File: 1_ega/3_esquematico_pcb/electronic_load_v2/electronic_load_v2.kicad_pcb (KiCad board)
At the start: 2 copper layers, 100 x 100 mm, 65 parts, among them J1 Encoder, J10 5V, J11 LOAD, J12 Memoria SD, J13 LCD, J14 Io_sens, J15 VCC, J17 EGB_I2C, J18 EGB_UART, J2 RTC_I2C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

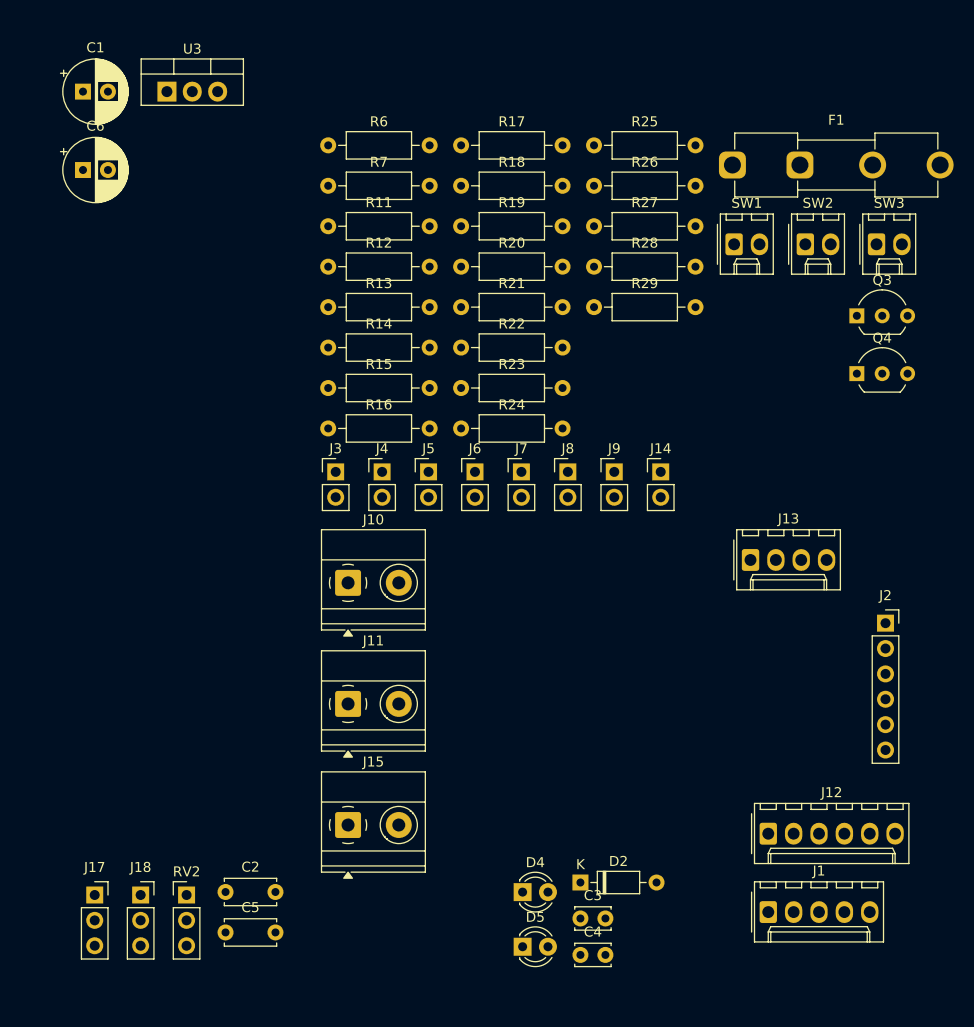
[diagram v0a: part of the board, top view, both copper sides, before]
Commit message: chore: pwm_offset con gpio
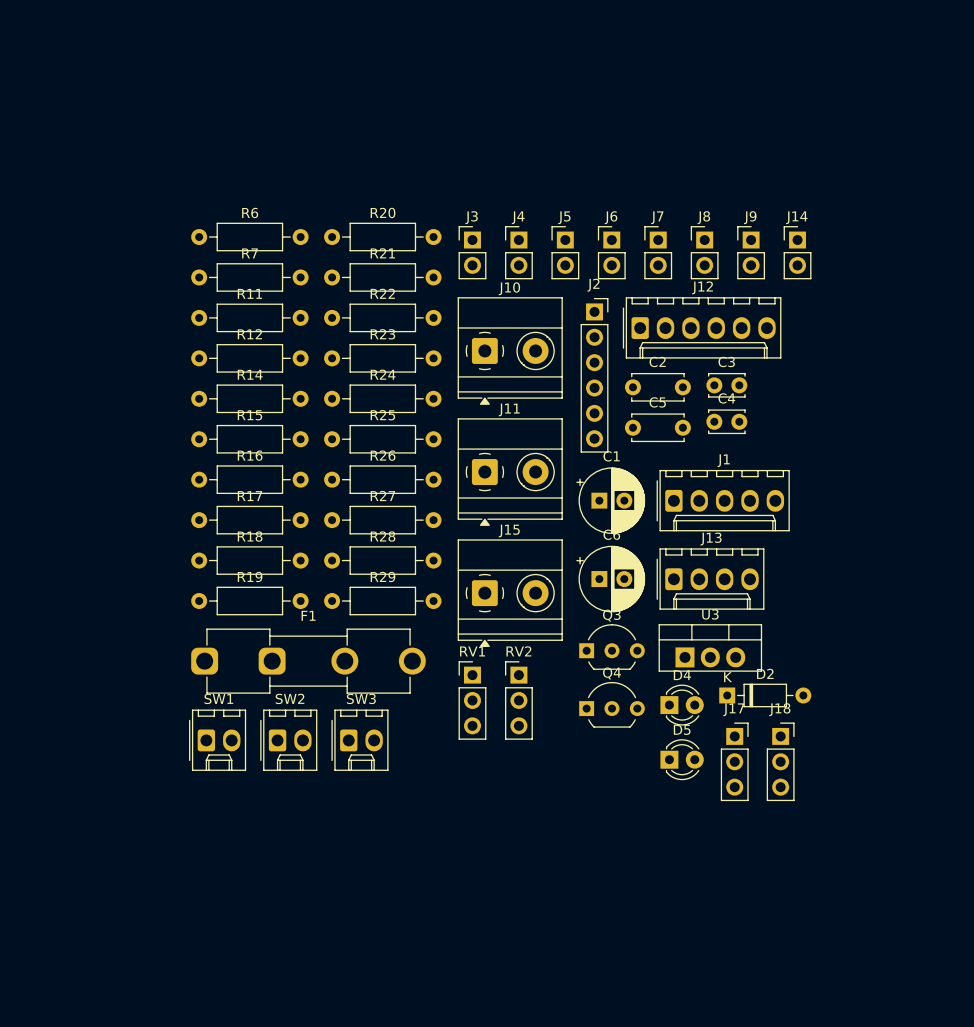
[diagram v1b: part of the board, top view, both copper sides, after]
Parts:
- removed R13: 6.8k, Resistor_THT:R_Axial_DIN0207_L6.3mm_D2.5mm_P10.16mm_Horizontal
- added RV1: 5k, Connector_PinHeader_2.54mm:PinHeader_1x03_P2.54mm_Vertical, F.Cu at (168.7, 83.9)
- R16: value 10k -> 4.7k
- moved U3 76.8 mm to (190.0, 82.1)
- moved F1 72.5 mm to (141.9, 82.5)
- moved SW1 72.5 mm to (142.1, 90.4)
- moved SW2 72.5 mm to (149.2, 90.4)
- moved SW3 72.5 mm to (156.3, 90.4)
- moved J17 66.0 mm to (195.0, 90.0)
- moved J18 66.0 mm to (199.6, 90.0)
- moved C1 66.0 mm to (181.4, 66.4)
- moved C6 66.0 mm to (181.4, 74.2)
- moved C2 65.0 mm to (184.8, 55.0)
- moved C5 65.0 mm to (184.8, 59.1)
- moved C4 55.0 mm to (192.9, 58.5)
- moved C3 55.0 mm to (192.9, 54.9)
- moved J12 52.2 mm to (185.5, 49.1)
- moved R18 45.8 mm to (141.3, 72.4)
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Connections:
- A1 pad 22: unconnected-(A1-GPIO17-Pad22) -> MOS_EN
- RV2 pad 1: Net-(R12-Pad1) -> MOS_EN
- RV2 pad 2: Net-(R12-Pad1) -> MOS_OFFSET
- RV2 pad 3: GND -> MOS_OFFSET

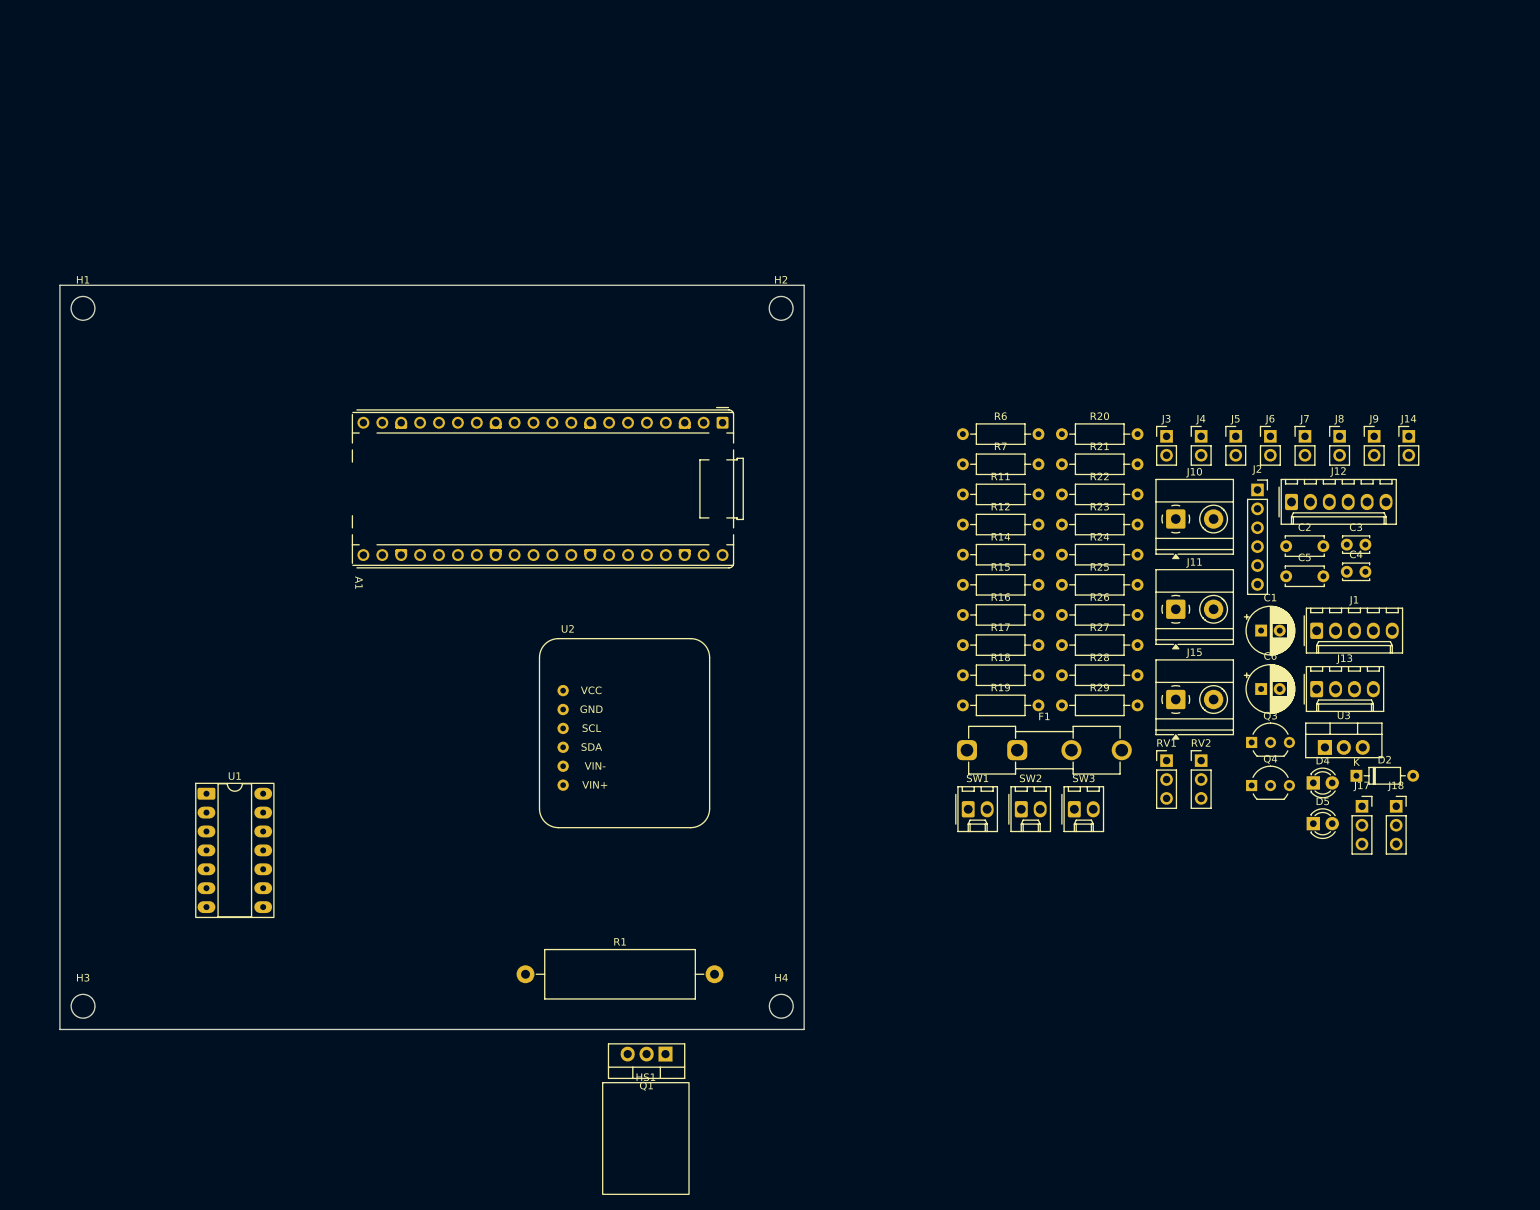
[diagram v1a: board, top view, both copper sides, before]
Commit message: perf: resistencias a huellas smd y preliminar de segunda version de pcb
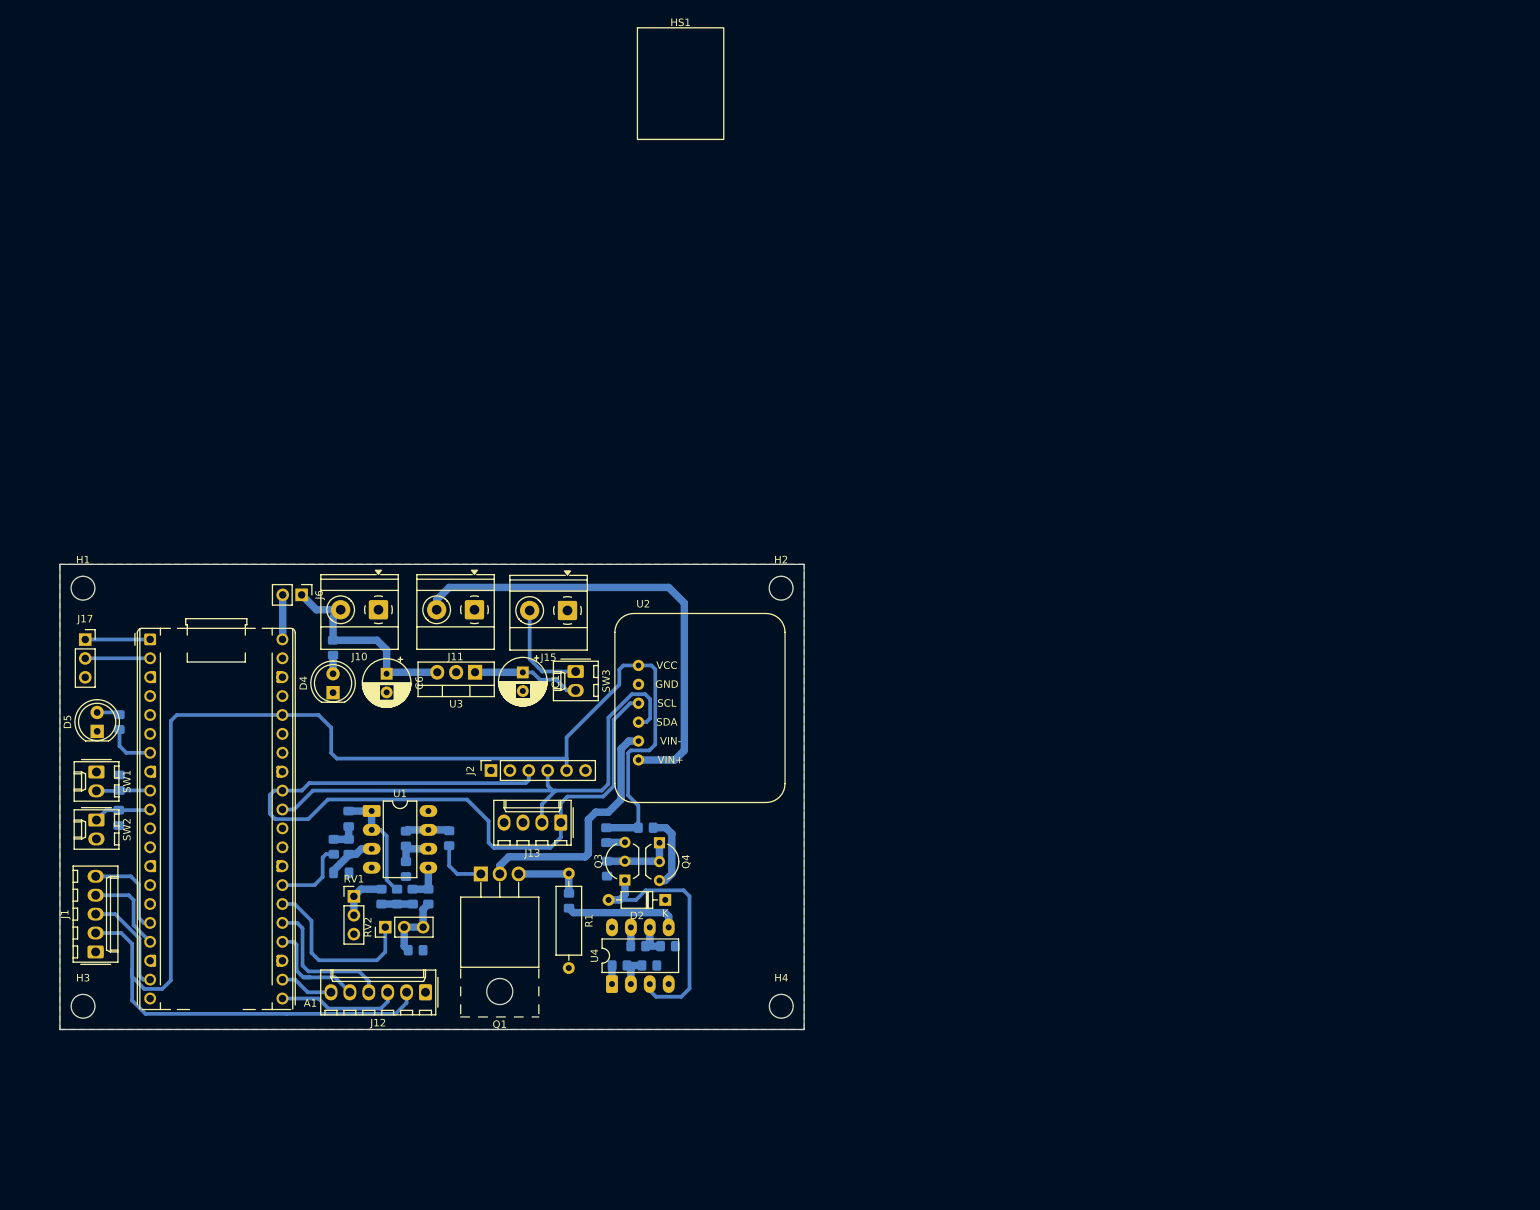
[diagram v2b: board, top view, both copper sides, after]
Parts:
- removed F1: Fuse, Fuse:Fuseholder_Clip-5x20mm_Eaton_1A5601-01_Inline_P20.80x6.76mm_D1.70mm_Horizontal
- removed J14: Io_sens, Connector_PinHeader_2.54mm:PinHeader_1x02_P2.54mm_Vertical
- removed J18: EGB_UART, Connector_PinSocket_2.54mm:PinSocket_1x03_P2.54mm_Vertical
- removed J3, J7: GND, Connector_PinHeader_2.54mm:PinHeader_1x02_P2.54mm_Vertical
- removed J4: MOS_GATE, Connector_PinHeader_2.54mm:PinHeader_1x02_P2.54mm_Vertical
- removed J5: MOS_PWM, Connector_PinHeader_2.54mm:PinHeader_1x02_P2.54mm_Vertical
- removed J8: OFFSET, Connector_PinHeader_2.54mm:PinHeader_1x02_P2.54mm_Vertical
- removed J9: TEMP_DIODE, Connector_PinHeader_2.54mm:PinHeader_1x02_P2.54mm_Vertical
- added U4: TL072, Package_DIP:DIP-8_W7.62mm_LongPads, F.Cu at (94.2, 113.9)
- C2, C5: footprint Capacitor_THT:C_Disc_D5.0mm_W2.5mm_P5.00mm -> Capacitor_SMD:C_0805_2012Metric_Pad1.18x1.45mm_HandSolder; moved to B.Cu
- C3, C4: footprint Capacitor_THT:C_Disc_D3.4mm_W2.1mm_P2.50mm -> Capacitor_SMD:C_0805_2012Metric_Pad1.18x1.45mm_HandSolder; moved to B.Cu
- D4, D5: footprint LED_THT:LED_D3.0mm -> LED_THT:LED_D5.0mm
- Q1: footprint Package_TO_SOT_THT:TO-220-3_Vertical -> Package_TO_SOT_THT:TO-220F-3_Horizontal_TabUp
- R1: footprint Resistor_THT:R_Axial_Power_L20.0mm_W6.4mm_P25.40mm -> Resistor_THT:R_Axial_DIN0309_L9.0mm_D3.2mm_P12.70mm_Horizontal
- R11, R12, R14, R15, R16, R17, R18, R19, R20, R21, R22, R23, R24, R25, R26, R27, R28, R29, R6, R7: footprint Resistor_THT:R_Axial_DIN0207_L6.3mm_D2.5mm_P10.16mm_Horizontal -> Resistor_SMD:R_0805_2012Metric_Pad1.20x1.40mm_HandSolder; moved to B.Cu
- U1: value TL074 -> TL072; footprint Package_DIP:DIP-14_W7.62mm_Socket_LongPads -> Package_DIP:DIP-8_W7.62mm_LongPads
- moved J17 173.0 mm to (23.4, 67.6)
- moved J1 169.7 mm to (24.8, 109.6), turned to 90 degrees
- moved C4 168.3 mm to (27.9, 91.6), turned to 90 degrees
- moved C3 168.0 mm to (28.0, 86.8), turned to -90 degrees
- moved D5 163.9 mm to (25.0, 79.9), turned to 90 degrees
- moved HS1 141.8 mm to (103.4, -14.8)
- moved C2 134.3 mm to (57.8, 99.0)
- moved J12 133.7 mm to (69.1, 115.0), turned to 180 degrees
- moved D4 132.3 mm to (56.7, 74.7), turned to 90 degrees
- moved J6 131.9 mm to (52.5, 61.6), turned to -90 degrees
- moved C5 130.1 mm to (58.8, 91.7), turned to 90 degrees
- moved R28 126.8 mm to (28.0, 78.7), turned to 90 degrees
- moved SW2 124.3 mm to (24.9, 91.9), turned to -90 degrees
- moved C6 117.5 mm to (63.9, 72.2), turned to -90 degrees
- moved SW1 117.3 mm to (24.9, 85.4), turned to -90 degrees
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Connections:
- A1 pad 1: unconnected-(A1-GPIO0-Pad1) -> EGB_TX_SDA
- A1 pad 14: I2C1_SCL -> unconnected-(A1-GPIO10-Pad14)
- A1 pad 15: I2C1_SDA -> unconnected-(A1-GPIO11-Pad15)
- A1 pad 2: SPI0_CS -> EGB_RX_SCL
- A1 pad 20: LED_ACTIVE -> unconnected-(A1-GPIO15-Pad20)
- A1 pad 21: MOS_PWM -> SPI0_RX
- A1 pad 22: MOS_EN -> SPI0_CS
- A1 pad 24: I2C_SDA -> SPI0_CLK
- A1 pad 25: I2C_SCL -> SPI0_TX
- A1 pad 26: RTC_SQW -> MOS_EN
- A1 pad 27: RTC_32K -> MOS_PWM
- A1 pad 31: TEMP_DIODE -> I2C_SDA
- A1 pad 32: unconnected-(A1-GPIO27_ADC1-Pad32) -> I2C_SCL
- A1 pad 34: unconnected-(A1-GPIO28_ADC2-Pad34) -> TEMP_DIODE
- A1 pad 4: SPI0_CLK -> unconnected-(A1-GPIO2-Pad4)
- A1 pad 5: SPI0_TX -> unconnected-(A1-GPIO3-Pad5)
- A1 pad 6: SPI0_RX -> unconnected-(A1-GPIO4-Pad6)
- A1 pad 7: unconnected-(A1-GPIO5-Pad7) -> LED_ACTIVE
- J11 pad 2: Net-(J11-Pin_2) -> LOAD+
- J17 pad 1: I2C1_SCL -> EGB_TX_SDA
- J17 pad 2: I2C1_SDA -> EGB_RX_SCL
- R14 pad 1: Net-(U1C--) -> Net-(U4A--)
- R15 pad 1: Net-(U1C--) -> Net-(U4A--)
- R25 pad 2: Net-(U1D-+) -> Net-(U4B-+)
- R26 pad 2: Net-(U1D--) -> Net-(U4B--)
- R29 pad 1: Net-(U1D--) -> Net-(U4B--)
- U1 pad 4: VCC -> GND
- U1 pad 8: TEMP_DIODE -> VCC
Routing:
- net +3V3: track 0.00 -> 203.7 mm
- net I2C_SCL: track 0.00 -> 110.7 mm
- net I2C_SDA: track 0.00 -> 73.7 mm
- net LOAD+: track 0.00 -> 62.7 mm
- net Net-(D2-A): track 0.00 -> 35.6 mm
- net MOS_DRAIN: track 0.00 -> 33.4 mm
- net +5V: track 0.00 -> 28.4 mm
- net MOS_EN: track 0.00 -> 23.3 mm
- net SPI0_TX: track 0.00 -> 19.3 mm
- net SPI0_RX: track 0.00 -> 16.4 mm
- net Net-(U1A--): track 0.00 -> 15.8 mm
- net Net-(U4B-+): track 0.00 -> 15.3 mm
- net VCC: track 0.00 -> 14.9 mm
- net SPI0_CLK: track 0.00 -> 14.7 mm
- net ENC_SW: track 0.00 -> 13.9 mm
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- added copper zone on B.Cu, net GND
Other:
- board size 100 x 100 mm -> 100 x 62.5 mm
